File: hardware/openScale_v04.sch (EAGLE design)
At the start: 72 parts, among them J1 3.3V, J2 UL, J3 UR, J4 LL, J5 LR, Q1 200mA/50V, Q2 200mA/50V, Q3 MMBT4403, Q4 MOSFET-NCHANNEL2N7002PW, U1 HX711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

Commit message: Updated Board and Schematic files per QC checklist
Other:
- note added: "Default :Left side of Jumper closed to provide 5V to DVDD. Customer to close right side and provide 3.3V to J1."
- note removed: "Default: Jumper closed to provide 5V to DVDD. Solder tother side open currently soldered side for 3.3V to be supplied by customer."
- moved on the sheet: R11, R12
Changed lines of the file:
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@@
 <text x="205.74" y="27.94" size="3.81" layer="97">Combine 4 Load sensors to create 1 load cell</text>
 <text x="185.42" y="78.74" size="5.08" layer="97" font="vector">Load Sensor Combiner</text>
-<text x="139.7" y="251.46" size="1.778" layer="97">Default: Jumper closed to provide 5V to DVDD.
-Solder tother side open currently soldered side
-for 3.3V to be supplied by customer. </text>
+<text x="160.02" y="248.92" size="1.778" layer="97">Default :Left side of Jumper closed to provide 5V to DVDD.
+Customer to close right side and provide 3.3V to J1. </text>
 <text x="331.47" y="7.366" size="2.54" layer="94">Revision by:   Mary West</text>
 <wire x1="0" y1="160.02" x2="180.34" y2="160.02" width="0.1524" layer="97" style="shortdash"/>
@@
 <instance part="U$16" gate="G$1" x="269.24" y="220.98"/>
 <instance part="GND1" gate="1" x="266.7" y="190.5"/>
-<instance part="U3" gate="G$1" x="337.82" y="210.82"/>
+<instance part="U3" gate="G$1" x="337.82" y="210.82" smashed="yes">
+<attribute name="NAME" x="330.2" y="219.202" size="1.778" layer="95"/>
+<attribute name="VALUE" x="330.2" y="200.66" size="1.778" layer="96"/>
+</instance>
 <instance part="GND18" gate="1" x="322.58" y="200.66"/>
 <instance part="C3" gate="G$1" x="312.42" y="208.28"/>
@@
 <instance part="U$10" gate="G$1" x="149.86" y="132.08"/>
 <instance part="GND13" gate="1" x="149.86" y="111.76"/>
-<instance part="R11" gate="G$1" x="322.58" y="154.94" rot="R180"/>
-<instance part="R12" gate="G$1" x="325.12" y="147.32" rot="R180"/>
+<instance part="R11" gate="G$1" x="327.66" y="154.94" rot="R180"/>
+<instance part="R12" gate="G$1" x="330.2" y="147.32" rot="R180"/>
 <instance part="U4" gate="U$1" x="101.6" y="73.66"/>
 <instance part="Q1" gate="G$1" x="365.76" y="215.9" smashed="yes" rot="R270">
@@
 </segment>
 <segment>
-<label x="330.2" y="154.94" size="1.27" layer="95" xref="yes"/>
+<label x="337.82" y="154.94" size="1.27" layer="95" xref="yes"/>
 <pinref part="R11" gate="G$1" pin="1"/>
-<wire x1="327.66" y1="154.94" x2="330.2" y2="154.94" width="0.1524" layer="91"/>
+<wire x1="332.74" y1="154.94" x2="337.82" y2="154.94" width="0.1524" layer="91"/>
 </segment>
 <segment>
@@
 </segment>
 <segment>
-<label x="332.74" y="147.32" size="1.27" layer="95" xref="yes"/>
-<wire x1="330.2" y1="147.32" x2="332.74" y2="147.32" width="0.1524" layer="91"/>
+<label x="337.82" y="147.32" size="1.27" layer="95" xref="yes"/>
+<wire x1="335.28" y1="147.32" x2="337.82" y2="147.32" width="0.1524" layer="91"/>
 <pinref part="R12" gate="G$1" pin="1"/>
 </segment>
@@
 <segment>
 <pinref part="Q4" gate="G$1" pin="D"/>
-<wire x1="340.36" y1="127" x2="347.98" y2="127" width="0.2032" layer="91"/>
+<wire x1="340.36" y1="127" x2="347.98" y2="127" width="0.1524" layer="91"/>
 <pinref part="R18" gate="G$1" pin="1"/>
-<wire x1="347.98" y1="127" x2="353.06" y2="127" width="0.2032" layer="91"/>
-<wire x1="347.98" y1="129.54" x2="347.98" y2="127" width="0.2032" layer="91"/>
+<wire x1="347.98" y1="127" x2="353.06" y2="127" width="0.1524" layer="91"/>
+<wire x1="347.98" y1="129.54" x2="347.98" y2="127" width="0.1524" layer="91"/>
 <junction x="347.98" y="127"/>
 <label x="353.06" y="127" size="1.27" layer="95" xref="yes"/>
@@
 <pinref part="U$13" gate="G$1" pin="5V"/>
 <pinref part="R18" gate="G$1" pin="2"/>
-<wire x1="347.98" y1="142.24" x2="347.98" y2="139.7" width="0.2032" layer="91"/>
+<wire x1="347.98" y1="142.24" x2="347.98" y2="139.7" width="0.1524" layer="91"/>
 </segment>
 </net>
@@
 <net name="N$16" class="0">
 <segment>
-<pinref part="R11" gate="G$1" pin="2"/>
-<wire x1="317.5" y1="154.94" x2="317.5" y2="139.7" width="0.1524" layer="91"/>
 <wire x1="314.96" y1="139.7" x2="317.5" y2="139.7" width="0.1524" layer="91"/>
 <pinref part="U6" gate="U$1" pin="TXD"/>
+<pinref part="R11" gate="G$1" pin="2"/>
+<wire x1="322.58" y1="154.94" x2="317.5" y2="154.94" width="0.1524" layer="91"/>
+<wire x1="317.5" y1="154.94" x2="317.5" y2="139.7" width="0.1524" layer="91"/>
 </segment>
 </net>
@@
 <net name="N$22" class="0">
 <segment>
+<wire x1="266.7" y1="40.64" x2="266.7" y2="43.18" width="0.1524" layer="91"/>
+<pinref part="J4" gate="J$1" pin="1"/>
+<wire x1="266.7" y1="45.72" x2="266.7" y2="50.8" width="0.1524" layer="91"/>
+<wire x1="266.7" y1="50.8" x2="264.16" y2="50.8" width="0.1524" layer="91"/>
 <pinref part="J2" gate="J$1" pin="1"/>
-<wire x1="220.98" y1="60.96" x2="220.98" y2="43.18" width="0.1524" layer="91"/>
-<wire x1="220.98" y1="43.18" x2="266.7" y2="43.18" width="0.1524" layer="91"/>
-<wire x1="266.7" y1="43.18" x2="266.7" y2="50.8" width="0.1524" layer="91"/>
-<pinref part="J4" gate="J$1" pin="1"/>
-<wire x1="266.7" y1="50.8" x2="264.16" y2="50.8" width="0.1524" layer="91"/>
+<wire x1="220.98" y1="60.96" x2="231.14" y2="60.96" width="0.1524" layer="91"/>
+<wire x1="231.14" y1="60.96" x2="231.14" y2="40.64" width="0.1524" layer="91"/>
+<wire x1="231.14" y1="40.64" x2="266.7" y2="40.64" width="0.1524" layer="91"/>
+<wire x1="266.7" y1="43.18" x2="266.7" y2="45.72" width="0.1524" layer="91"/>
 </segment>
 </net>
@@
 <segment>
 <pinref part="U6" gate="U$1" pin="RXD"/>
-<wire x1="314.96" y1="137.16" x2="320.04" y2="137.16" width="0.2032" layer="91"/>
+<wire x1="314.96" y1="137.16" x2="320.04" y2="137.16" width="0.1524" layer="91"/>
 <pinref part="R12" gate="G$1" pin="2"/>
-<wire x1="320.04" y1="137.16" x2="320.04" y2="147.32" width="0.2032" layer="91"/>
+<wire x1="325.12" y1="147.32" x2="320.04" y2="147.32" width="0.1524" layer="91"/>
+<wire x1="320.04" y1="147.32" x2="320.04" y2="137.16" width="0.1524" layer="91"/>
 </segment>
 </net>
@@
 <segment>
 <pinref part="Q4" gate="G$1" pin="G"/>
-<wire x1="335.28" y1="134.62" x2="335.28" y2="142.24" width="0.2032" layer="91"/>
-<wire x1="335.28" y1="142.24" x2="325.12" y2="142.24" width="0.2032" layer="91"/>
+<wire x1="335.28" y1="134.62" x2="335.28" y2="142.24" width="0.1524" layer="91"/>
+<wire x1="335.28" y1="142.24" x2="325.12" y2="142.24" width="0.1524" layer="91"/>
 <pinref part="R10" gate="G$1" pin="2"/>
-<wire x1="325.12" y1="142.24" x2="325.12" y2="139.7" width="0.2032" layer="91"/>
-</segment>
-</net>
+<wire x1="325.12" y1="142.24" x2="325.12" y2="139.7" width="0.1524" layer="91"/>
+</segment>
+</net>

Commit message: Updated yellow LED
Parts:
- D1: value YELLOW -> Yellow; device SparkFun-LED:LED-YELLOW1206 -> SparkFun-LED:LED-YELLOWLILYPAD
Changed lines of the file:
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@@
 <part name="GND21" library="SparkFun" deviceset="GND" device=""/>
 <part name="GND22" library="SparkFun" deviceset="GND" device=""/>
-<part name="D1" library="SparkFun-LED" deviceset="LED-YELLOW" device="1206" value="YELLOW"/>
+<part name="D1" library="SparkFun-LED" deviceset="LED-YELLOW" device="LILYPAD" value="Yellow"/>
 <part name="D2" library="SparkFun-LED" deviceset="LED-GREEN" device="1206" value="GREEN"/>
 <part name="U$1" library="SparkFun" deviceset="5V" device=""/>

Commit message: Updated Board and Schemtic
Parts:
- added C14: 0.1uF, SparkFun-Capacitors:0.1UF-25V(+80/-20%)(0603)
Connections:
- removed net N$33: Q4.G, R10.2
- net 3.3V: now also Q4.G, R10.2
- net GND: now also C14.2
- net N$12: now also C14.1
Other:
- moved on the sheet: C10, C2, C5, C7, C9, D1, D2, F1, JP7, R1, R10, R11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

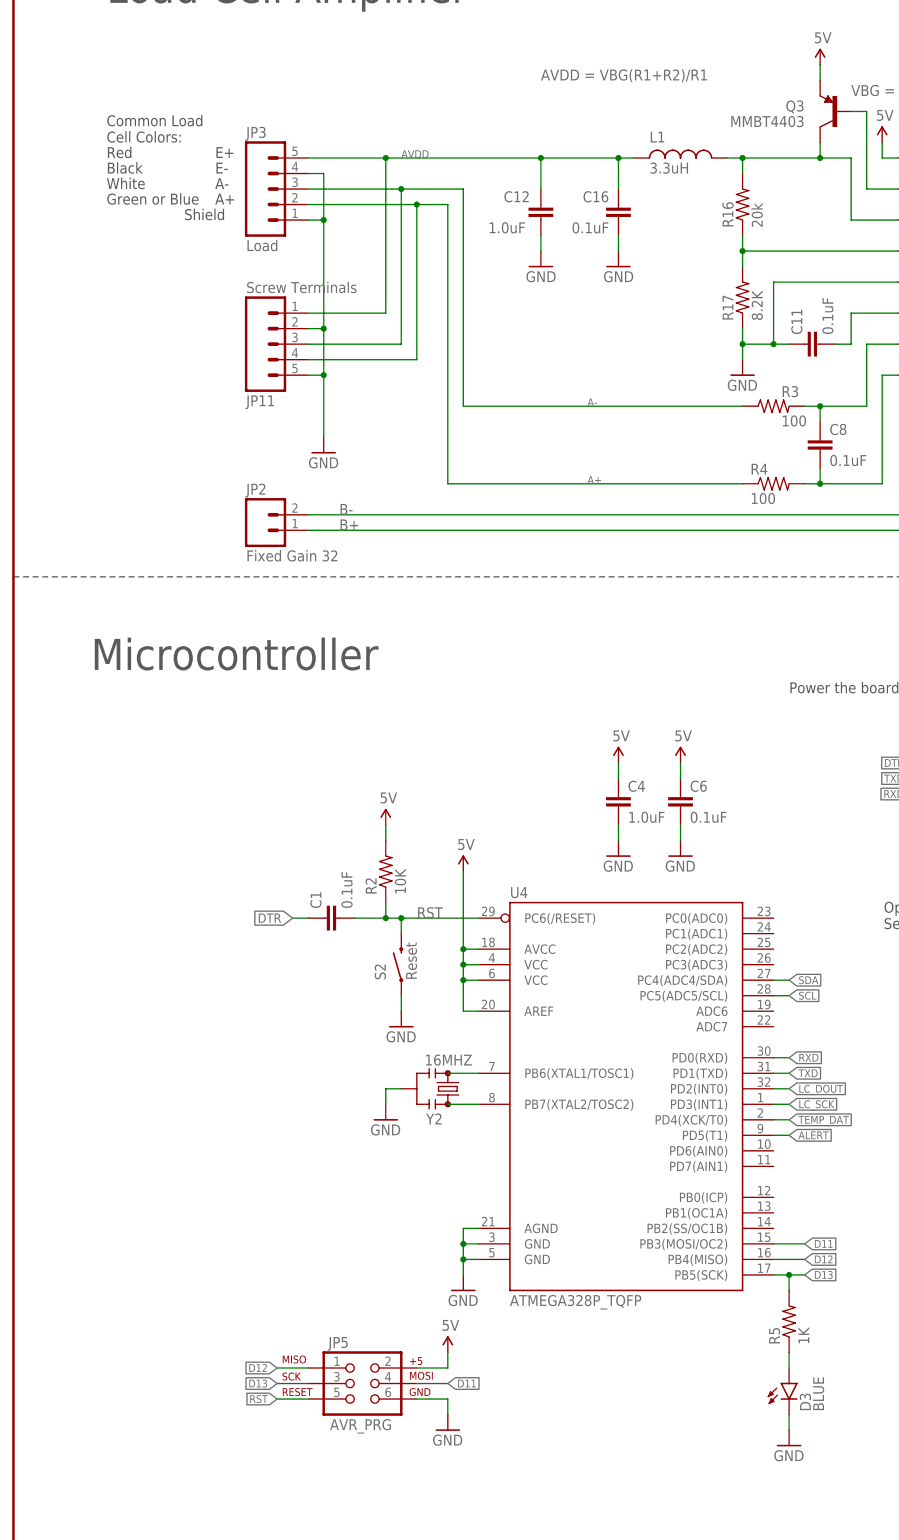
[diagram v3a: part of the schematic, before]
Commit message: Updated BRD and SCH file per Engineering Design Review
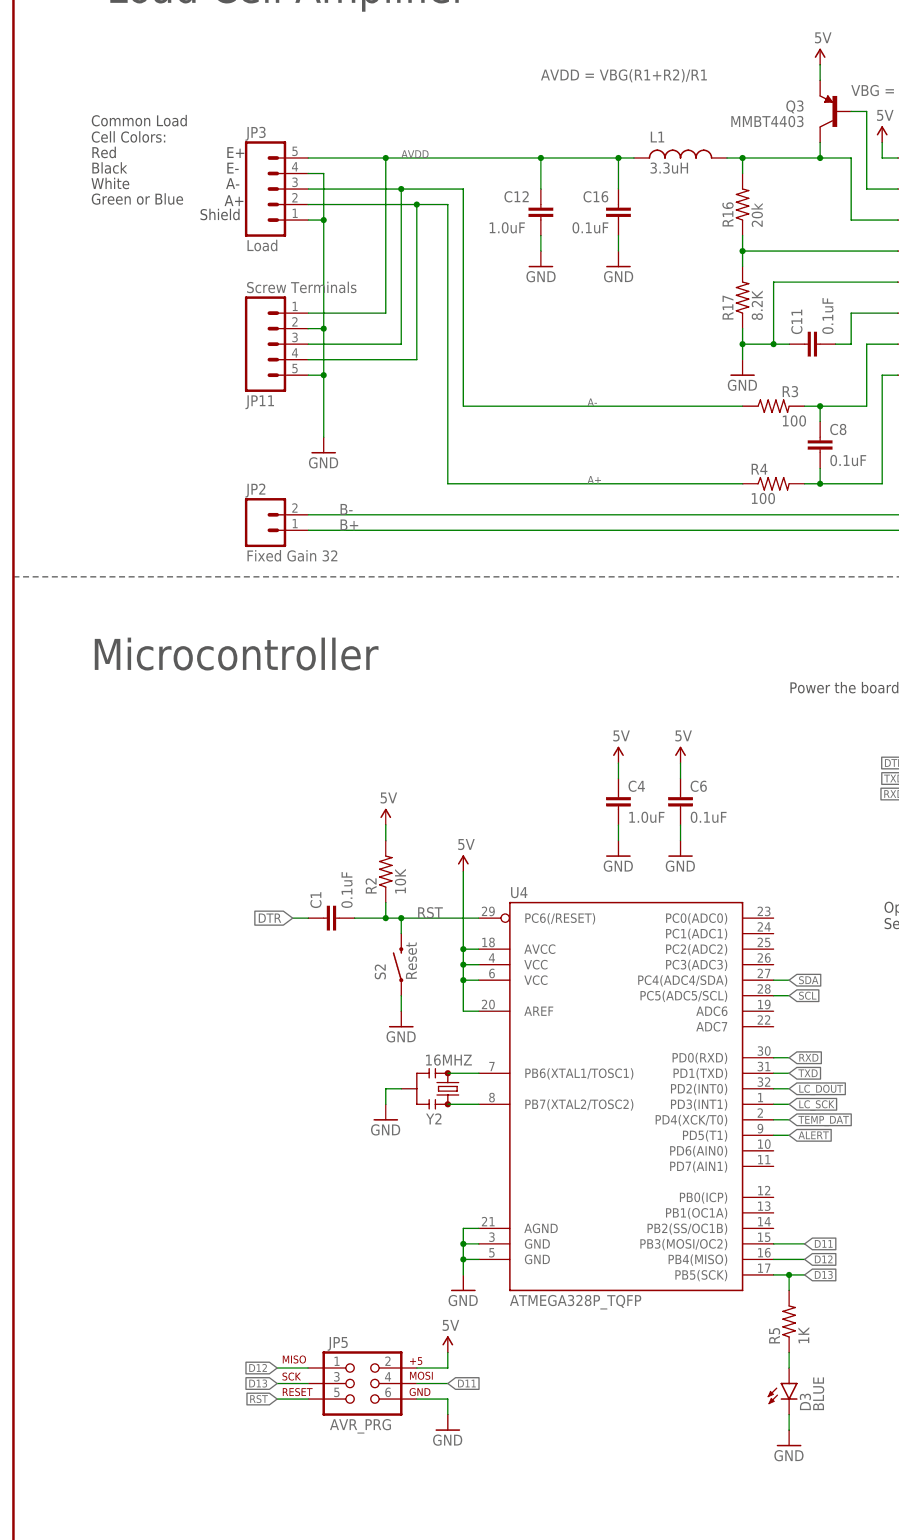
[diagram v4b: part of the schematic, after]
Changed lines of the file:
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@@
 </classes>
 <parts>
-<part name="GND2" library="SparkFun" deviceset="GND" device=""/>
 <part name="GND5" library="SparkFun" deviceset="GND" device=""/>
 <part name="GND6" library="SparkFun" deviceset="GND" device=""/>
@@
 <part name="GND24" library="SparkFun" deviceset="GND" device=""/>
 <part name="P+1" library="SparkFun-Aesthetics" deviceset="3.3V" device="" value="3.3V"/>
+<part name="GND2" library="SparkFun-Aesthetics" deviceset="GND" device=""/>
 </parts>
 <sheets>
 <sheet>
 <plain>
-<text x="12.7" y="144.78" size="5.08" layer="97">Microcontroller</text>
-<text x="182.88" y="149.86" size="5.08" layer="97">USB-Serial</text>
-<text x="200.66" y="218.44" size="1.778" layer="97">Default: Closed/Data rate 10SPS</text>
-<text x="200.66" y="213.36" size="1.778" layer="97">Open jumper to set to 80SPS
+<text x="12.7" y="144.78" size="5.08" layer="97" font="vector">Microcontroller</text>
+<text x="182.88" y="149.86" size="5.08" layer="97" font="vector">USB-Serial</text>
+<text x="200.66" y="218.44" size="1.778" layer="97" font="vector">Default: Closed/Data rate 10SPS</text>
+<text x="200.66" y="213.36" size="1.778" layer="97" font="vector">Open jumper to set to 80SPS
 Noise floor doubles to 90nV</text>
-<text x="33.02" y="228.6" size="1.778" layer="97">E+</text>
-<text x="33.02" y="226.06" size="1.778" layer="97">E-</text>
-<text x="33.02" y="223.52" size="1.778" layer="97">A-</text>
-<text x="33.02" y="220.98" size="1.778" layer="97">A+</text>
-<text x="15.24" y="228.6" size="1.778" layer="97">Red</text>
-<text x="15.24" y="226.06" size="1.778" layer="97">Black</text>
-<text x="15.24" y="223.52" size="1.778" layer="97">White</text>
-<text x="15.24" y="220.98" size="1.778" layer="97">Green or Blue</text>
-<text x="15.24" y="231.14" size="1.778" layer="97">Common Load
+<text x="34.798" y="228.6" size="1.778" layer="97">E+</text>
+<text x="34.798" y="226.06" size="1.778" layer="97">E-</text>
+<text x="34.798" y="223.52" size="1.778" layer="97">A-</text>
+<text x="34.544" y="220.726" size="1.778" layer="97">A+</text>
+<text x="12.7" y="228.6" size="1.778" layer="97" font="vector">Red</text>
+<text x="12.7" y="226.06" size="1.778" layer="97" font="vector">Black</text>
+<text x="12.7" y="223.52" size="1.778" layer="97" font="vector">White</text>
+<text x="12.7" y="220.98" size="1.778" layer="97" font="vector">Green or Blue</text>
+<text x="12.7" y="231.14" size="1.778" layer="97" font="vector">Common Load
 Cell Colors:</text>
-<text x="251.46" y="264.16" size="5.08" layer="97">Temperature Compensation</text>
-<text x="240.792" y="197.358" size="2.54" layer="97">(Optional)
+<text x="251.46" y="264.16" size="5.08" layer="97" font="vector">Temperature Compensation</text>
+<text x="240.792" y="197.358" size="2.54" layer="97" font="vector">(Optional)
 External
 DS18B20</text>
-<text x="15.24" y="254" size="5.08" layer="97">Load Cell Amplifier</text>
-<text x="322.072" y="191.516" size="2.54" layer="97">7-Bit I2C: 0x49</text>
-<text x="27.94" y="218.44" size="1.778" layer="97">Shield</text>
-<text x="142.494" y="102.362" size="1.778" layer="97">Optional External
+<text x="15.24" y="254" size="5.08" layer="97" font="vector">Load Cell Amplifier</text>
+<text x="322.072" y="191.516" size="2.54" layer="97" font="vector">7-Bit I2C: 0x49</text>
+<text x="30.48" y="218.44" size="1.778" layer="97">Shield</text>
+<text x="142.494" y="102.362" size="1.778" layer="97" font="vector">Optional External
 Serial Interface</text>
 <text x="137.16" y="238.76" size="1.778" layer="96">VBG = 1.25V</text>
-<text x="86.36" y="241.3" size="1.778" layer="96">AVDD = VBG(R1+R2)/R1</text>
-<text x="421.64" y="7.62" size="2.54" layer="94">v04</text>
-<text x="353.568" y="11.43" size="2.54" layer="94">N. Seidle</text>
+<text x="86.36" y="241.3" size="1.778" layer="96" font="vector">AVDD = VBG(R1+R2)/R1</text>
+<text x="421.64" y="7.62" size="2.54" layer="94" font="vector">v04</text>
+<text x="353.568" y="11.43" size="2.54" layer="94" font="vector">N. Seidle</text>
 <text x="127" y="140.97" size="1.778" layer="97">Power the board with 4.5-5.5V</text>
 <text x="205.74" y="66.04" size="1.778" layer="97" font="vector">RED</text>
 <text x="205.74" y="63.5" size="1.778" layer="97" font="vector">WHT</text>
 <text x="205.74" y="60.96" size="1.778" layer="97" font="vector">BLK</text>
-<text x="205.74" y="27.94" size="3.81" layer="97">Combine 4 Load sensors to create 1 load cell</text>
+<text x="205.74" y="27.94" size="3.81" layer="97" font="vector">Combine 4 Load sensors to create 1 load cell</text>
 <text x="185.42" y="78.74" size="5.08" layer="97" font="vector">Load Sensor Combiner</text>
-<text x="160.02" y="248.92" size="1.778" layer="97">Default :Left side of Jumper closed to provide 5V to DVDD.
+<text x="160.02" y="248.92" size="1.778" layer="97" font="vector">Default :Left side of Jumper closed to provide 5V to DVDD.
 Customer to close right side and provide 3.3V to J1. </text>
-<text x="331.47" y="7.366" size="2.54" layer="94">Revision by:   Mary West</text>
+<text x="331.47" y="7.366" size="2.54" layer="94" font="vector">Revision by:   Mary West</text>
 <wire x1="0" y1="160.02" x2="180.34" y2="160.02" width="0.1524" layer="97" style="shortdash"/>
 <wire x1="180.34" y1="160.02" x2="236.22" y2="160.02" width="0.1524" layer="97" style="shortdash"/>
@@
 </plain>
 <instances>
-<instance part="GND2" gate="1" x="127" y="17.78"/>
 <instance part="GND5" gate="1" x="73.66" y="43.18"/>
 <instance part="GND6" gate="1" x="63.5" y="86.36"/>
@@
 <instance part="GND24" gate="1" x="213.36" y="93.98"/>
 <instance part="P+1" gate="G$1" x="317.5" y="134.62"/>
+<instance part="GND2" gate="1" x="127" y="17.78"/>
 </instances>
 <busses>
@@
 <nets>
 <net name="GND" class="1">
-<segment>
-<wire x1="127" y1="20.32" x2="127" y2="22.86" width="0.1524" layer="91"/>
-<pinref part="GND2" gate="1" pin="GND"/>
-<pinref part="D3" gate="G$1" pin="C"/>
-</segment>
 <segment>
 <pinref part="U4" gate="U$1" pin="GND@5"/>
@@
 <wire x1="213.36" y1="101.6" x2="213.36" y2="96.52" width="0.1524" layer="91"/>
 </segment>
+<segment>
+<pinref part="D3" gate="G$1" pin="C"/>
+<wire x1="127" y1="22.86" x2="127" y2="20.32" width="0.2032" layer="91"/>
+<pinref part="GND2" gate="1" pin="GND"/>
+</segment>
 </net>

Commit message: Updated Brd and Sch files per QC review.
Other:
- note added: "v10"
- note removed: "v04"
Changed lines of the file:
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@@
 <text x="137.16" y="238.76" size="1.778" layer="96">VBG = 1.25V</text>
 <text x="86.36" y="241.3" size="1.778" layer="96" font="vector">AVDD = VBG(R1+R2)/R1</text>
-<text x="421.64" y="7.62" size="2.54" layer="94" font="vector">v04</text>
+<text x="421.64" y="7.62" size="2.54" layer="94" font="vector">v10</text>
 <text x="353.568" y="11.43" size="2.54" layer="94" font="vector">N. Seidle</text>
 <text x="127" y="140.97" size="1.778" layer="97">Power the board with 4.5-5.5V</text>
@@
 <text x="205.74" y="63.5" size="1.778" layer="97" font="vector">WHT</text>
 <text x="205.74" y="60.96" size="1.778" layer="97" font="vector">BLK</text>
-<text x="205.74" y="27.94" size="3.81" layer="97" font="vector">Combine 4 Load sensors to create 1 load cell</text>
+<text x="210.82" y="25.4" size="2.54" layer="97" font="vector">Combine 4 Load sensors to create 1 load cell</text>
 <text x="185.42" y="78.74" size="5.08" layer="97" font="vector">Load Sensor Combiner</text>
 <text x="160.02" y="248.92" size="1.778" layer="97" font="vector">Default :Left side of Jumper closed to provide 5V to DVDD.
